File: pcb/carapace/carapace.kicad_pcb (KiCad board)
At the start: 2 copper layers, 21.5 x 48 mm, 10 parts, among them J2 Würth 61201621721, P1 Qwiic verso X20, P2 catena LED, P3 microfoni, P4 amplificatore, P5 ToF posteriore, P6 pulsante, P7 riserva polo 14

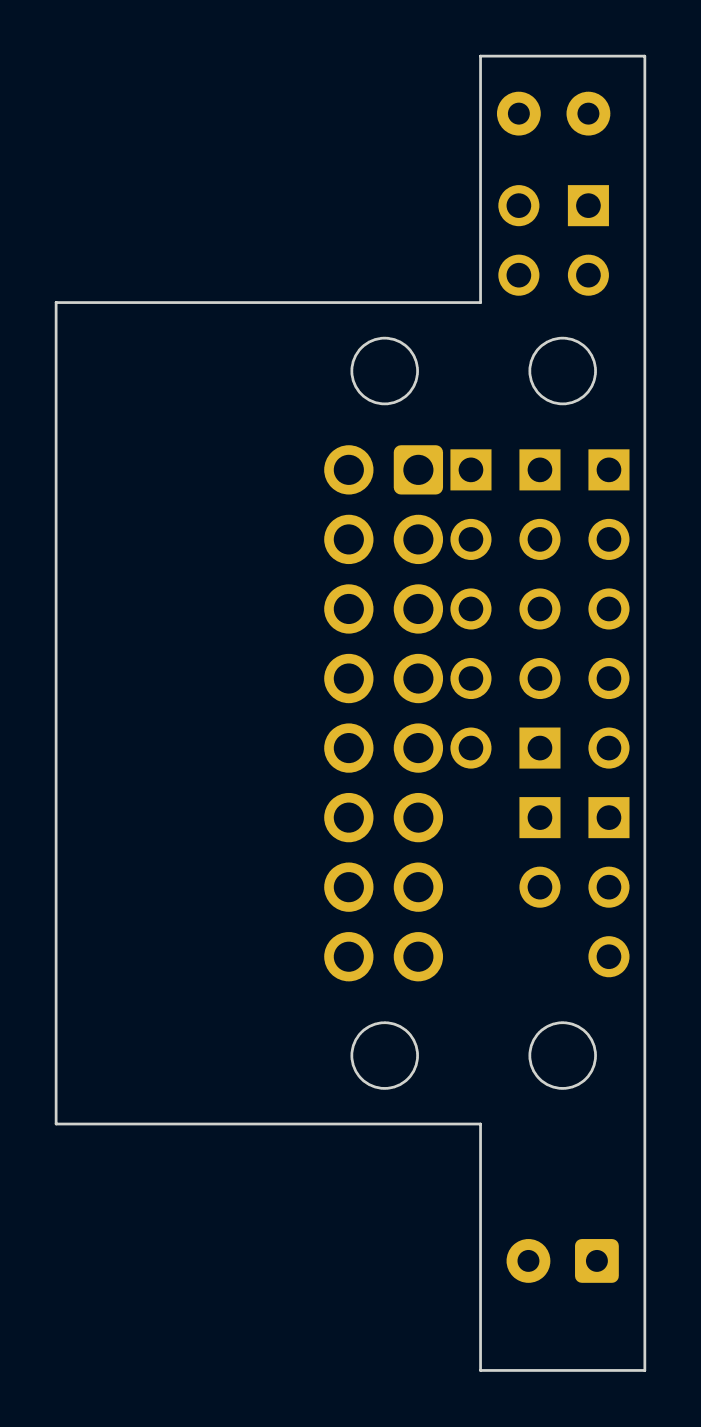
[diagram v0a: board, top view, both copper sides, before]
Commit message: D-082: correzioni della revisione indipendente (17 agenti): PCB-C rifatta e sbrogliata da script (DRC a zero), regole del DRC corrette (una scritta male faceva ignorare il file), piazzole dei fili in verifica_reti, ali da 5,5, JP-RMT 680/1k, tetto dei LED 600/400 mA, guida 8.10/8.22/8.24, CI con KiCad obbligatorio; proposta della 2.1.9 (scheda dei partitori piu' grande)
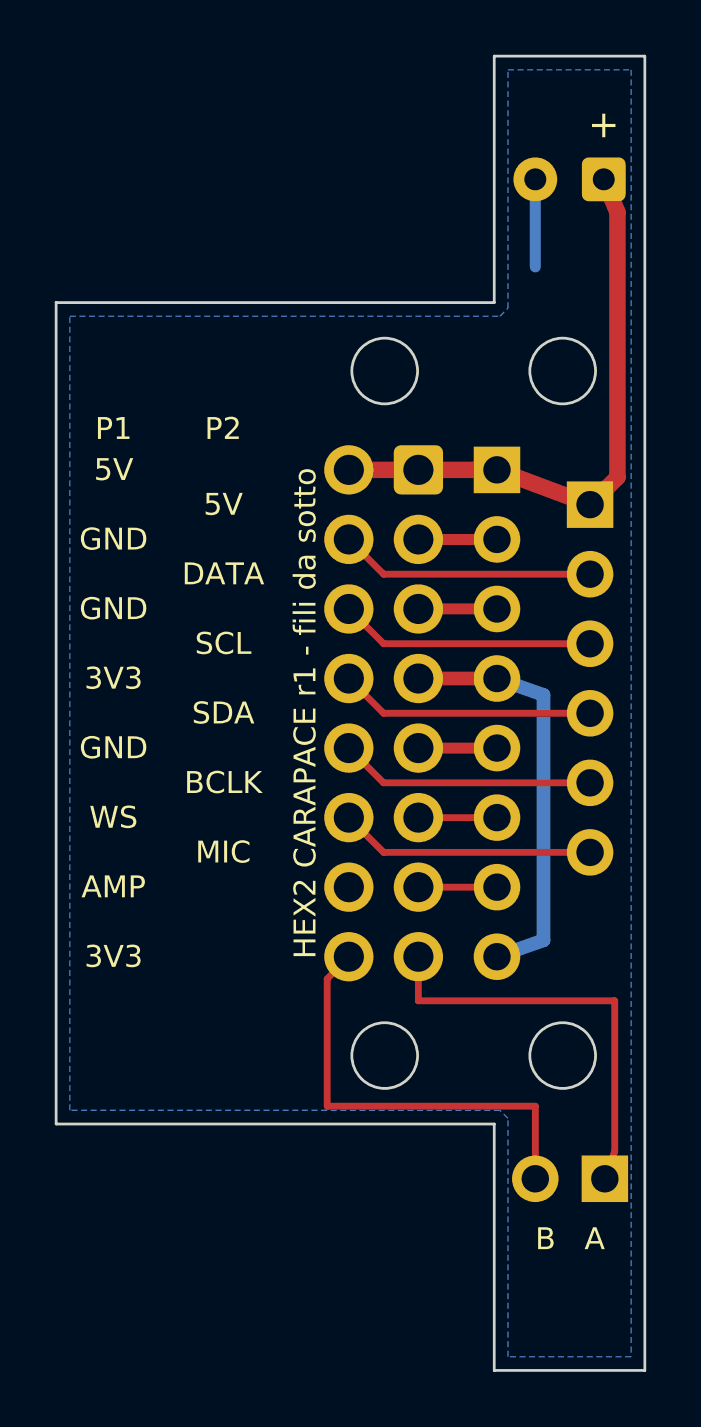
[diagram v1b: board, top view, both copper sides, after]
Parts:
- removed P4: amplificatore, hex2:Fili_1x05_P2.54mm_D1.5
- removed P5: ToF posteriore, hex2:Fili_2x02_P2.54mm_D1.5
- removed P6: pulsante, hex2:Fili_1x02_P2.54mm_D1.5
- removed P7: riserva polo 14, hex2:Fili_1x01_P2.54mm_D1.5
- removed R1: R-MIC, hex2:R_Axial_DIN0207_L6.3mm_D2.5mm_P2.54mm_Vertical
- P1: value Qwiic verso X20 -> poli dispari; footprint hex2:Fili_1x04_P2.54mm_D1.5 -> hex2:Fili_1x08_P2.54mm_D1.7
- P2: value catena LED -> poli pari; footprint hex2:Fili_1x03_P2.54mm_D1.5 -> hex2:Fili_1x06_P2.54mm_D1.7
- P3: value microfoni -> pulsante; footprint hex2:Fili_1x05_P2.54mm_D1.5 -> hex2:Fili_1x02_P2.54mm_D1.7
- moved CE1 39.5 mm to (149.5, 80.5)
- moved P3 26.3 mm to (149.5, 117.0), turned to 90 degrees
- moved P2 11.5 mm to (149.0, 92.4)
- moved P1 1.57 mm to (145.6, 91.1)
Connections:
- J2 pad 14: /RISERVA14 -> unconnected-(J2-Pin_14-Pad14)
- P1 pad 1: /GND -> /5V
- P1 pad 2: /3V3 -> /GND
- P1 pad 3: /SDA -> /GND
- P1 pad 4: /SCL -> /3V3
- P2 pad 3: /GND -> /SCL
- P3 pad 1: /3V3 -> /BTN_A
- P3 pad 2: /GND -> /BTN_B
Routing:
- net /5V: track 0.00 -> 21.4 mm
- net /BTN_B: track 0.00 -> 16.0 mm
- net /3V3: track 0.00 -> 15.4 mm
- net /BTN_A: track 0.00 -> 15.3 mm
- net /GND: track 0.00 -> 11.8 mm
- net /BCLK: track 0.00 -> 9.34 mm
- net /SDA: track 0.00 -> 9.34 mm
- net /SCL: track 0.00 -> 9.34 mm
- net /MIC: track 0.00 -> 9.34 mm
- net /DATA: track 0.00 -> 9.34 mm
- net /WS: track 0.00 -> 2.87 mm
- net /AMP: track 0.00 -> 2.87 mm
- added copper zone on B.Cu, net /GND
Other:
- outline, holes or cut-outs redrawn
- board text added: "+"
- board text added: "3V3"
- board text added: "5V"
- board text added: "AMP"
- board text added: "B A"
- board text added: "BCLK"
- board text added: "DATA"
- board text added: "GND"
- board text added: "HEX2 CARAPACE r1 - fili da sotto"
- board text added: "MIC"
- board text added: "P1"
- board text added: "P2"
- board text added: "SCL"
- board text added: "SDA"
- board text added: "WS"
